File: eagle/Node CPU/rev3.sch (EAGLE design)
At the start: 44 parts, among them IC1 MEGA8-AI

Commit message: updated to revision 3 of the board
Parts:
- removed PC0, PD0: (no value), pinhead:PINHD-1X1
- removed PWR: (no value), SparkFun-Passives:JUMPER-2PTH
- removed X1: (no value), con-wago-500:W237-102
- added C5: 22pF, resistor:C-EUC0603
- added GND_1, PC8, PD8: (no value), pinhead:PINHD-1X1
- added JP1: (no value), SparkFun-Connectors:M023.5MM
- added VCC_1: VCC, pinhead:PINHD-1X1
- C1: value 0.1uF -> 22pF
- C2: value 22pF -> 0.1uF
- IC1: value MEGA8-AI -> MEGA88
- MCP1: value (none) -> MCP2515
- MCP2: value MCP2551DIL8 -> MCP2551
- renumbered MCP2551 to MCP2
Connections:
- removed net N$36: MCP2G$1.CANL, X1-2.KL
- new net N$38: MCP1D.SO, MISO.1, R3.2
- new net N$39: IC1.PB5(SCK), ISP.4, R2.1
- net GND: now also C3.2, C5.1, GND_1.1; no longer C3.1, PWR.2
- net N$1: now also C1.1, IC1.AREF; no longer IC1.PB5(SCK), MCP1D.SCK, R2.1, SCK.1
- net N$10: now also JP1.1, MCP2G$1.CANL; no longer C3.2, IC1.PB6(XTAL1/TOSC1), XTAL.2
- net N$15: now also MCP1D.SCK, R2.2, SCK.1; no longer ISP.2, R4.2
- net N$16: now also JP1.2, MCP2G$1.CANH; no longer ISP.3, R3.2
- net N$17: now also IC1.PB3(MOSI/OC2), ISP.2, R4.1; no longer ISP.4, R2.2
- net N$2: now also ISP.3; no longer MCP1D.SO, MISO.1
- net N$20: now also PC2.1; no longer PC0.1
- net N$22: now also PC5.1; no longer PC2.1
- net N$23: now also PC6.1; no longer PC3.1
- net N$24: now also PC7.1; no longer PC4.1
- net N$25: now also PC8.1; no longer PC5.1
- net N$26: now also PC4.1; no longer PC6.1
- net N$27: now also PC3.1; no longer PC7.1
- net N$28: now also PD4.1; no longer PD0.1
- net N$29: now also PD5.1; no longer PD1.1
- net N$3: now also R4.2; no longer IC1.PB3(MOSI/OC2), R4.1
- net N$30: now also PD6.1; no longer PD2.1
- net N$31: now also PD7.1; no longer PD3.1
- net N$32: now also PD8.1; no longer PD4.1
- net N$33: now also PD3.1; no longer PD5.1
- net N$34: now also PD2.1; no longer PD6.1
- net N$35: now also PD1.1; no longer PD7.1
- net N$37: now also C4.2, IC1.PB6(XTAL1/TOSC1), XTAL.1; no longer MCP2G$1.CANH, X1-1.KL
- net N$9: now also C5.2, XTAL.2; no longer C4.2, XTAL.1
- net VCC: now also C3.1, VCC_1.1; no longer C1.1, PWR.1
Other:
- moved on the sheet: C1, C2, C3, C4, ISP, MISO, MOSI, PC2, PC3, PC4, PC5, PC6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

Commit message: update rev3 schematic
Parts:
- XTAL: device special:XTAL/S -> crystal:CRYSTALHC49S
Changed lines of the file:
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@@
 <attribute name="OC_NEWARK" value="unknown"/>
 </part>
-<part name="XTAL" library="special" deviceset="XTAL/S" device="" value="8MHz">
+<part name="XTAL" library="crystal" deviceset="CRYSTAL" device="HC49S" value="8MHz">
 <attribute name="MF" value=""/>
 <attribute name="MPN" value=""/>
@@
 <wire x1="58.42" y1="45.72" x2="58.42" y2="48.26" width="0.1524" layer="91"/>
 <pinref part="XTAL" gate="G$1" pin="2"/>
-<wire x1="58.42" y1="45.72" x2="50.8" y2="45.72" width="0.1524" layer="91"/>
+<wire x1="58.42" y1="45.72" x2="50.8" y2="48.26" width="0.1524" layer="91"/>
 <pinref part="C5" gate="G$1" pin="2"/>
-<wire x1="50.8" y1="45.72" x2="43.18" y2="45.72" width="0.1524" layer="91"/>
-<junction x="50.8" y="45.72"/>
+<wire x1="50.8" y1="48.26" x2="43.18" y2="45.72" width="0.1524" layer="91"/>
+<junction x="50.8" y="48.26"/>
 </segment>
 </net>
@@
 <pinref part="C4" gate="G$1" pin="2"/>
 <pinref part="XTAL" gate="G$1" pin="1"/>
-<wire x1="43.18" y1="55.88" x2="50.8" y2="55.88" width="0.1524" layer="91"/>
+<wire x1="43.18" y1="55.88" x2="50.8" y2="53.34" width="0.1524" layer="91"/>
 <pinref part="IC1" gate="G$1" pin="PB6(XTAL1/TOSC1)"/>
 <wire x1="58.42" y1="53.34" x2="58.42" y2="55.88" width="0.1524" layer="91"/>
-<wire x1="50.8" y1="55.88" x2="58.42" y2="55.88" width="0.1524" layer="91"/>
-<junction x="50.8" y="55.88"/>
-</segment>
-</net>
+<wire x1="50.8" y1="53.34" x2="58.42" y2="55.88" width="0.1524" layer="91"/>
+<junction x="50.8" y="53.34"/>
+</segment>
+</net>

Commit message: update rev3 board schematic
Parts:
- removed PC6, PC7, PC8, PD8: (no value), pinhead:PINHD-1X1
- added ADC6, ADC7, PC0, PD0: (no value), pinhead:PINHD-1X1
- added C6, C7: 0.1uF, resistor:C-EUC0603
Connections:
- net GND: now also C6.2, C7.2, MCP1P.GND, MCP2G$2.GND
- net N$20: now also PC0.1; no longer PC2.1
- net N$22: now also PC2.1; no longer PC5.1
- net N$23: now also PC3.1; no longer PC6.1
- net N$24: now also PC4.1; no longer PC7.1
- net N$25: now also PC5.1; no longer PC8.1
- net N$26: now also ADC6.1; no longer PC4.1
- net N$27: now also ADC7.1; no longer PC3.1
- net N$28: now also PD0.1; no longer PD4.1
- net N$29: now also PD1.1; no longer PD5.1
- net N$30: now also PD2.1; no longer PD6.1
- net N$31: now also PD3.1; no longer PD7.1
- net N$32: now also PD4.1; no longer PD8.1
- net N$33: now also PD5.1; no longer PD3.1
- net N$34: now also PD6.1; no longer PD2.1
- net N$35: now also PD7.1; no longer PD1.1
- net VCC: now also C6.1, C7.1, MCP1P.VCC, MCP2G$2.VCC
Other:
- moved on the sheet: C4, C5, PC2, PC3, PC4, PC5, PD1, PD2, PD3, PD4, PD5, PD6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

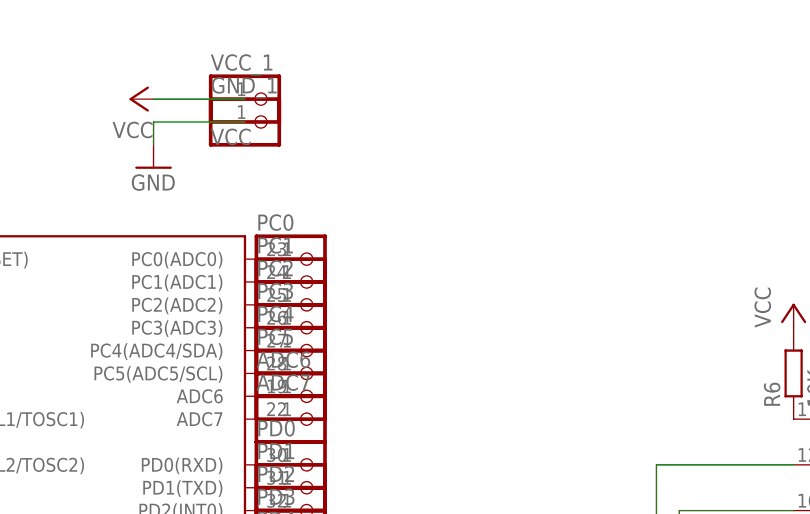
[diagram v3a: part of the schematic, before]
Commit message: add power LED to node cpu board
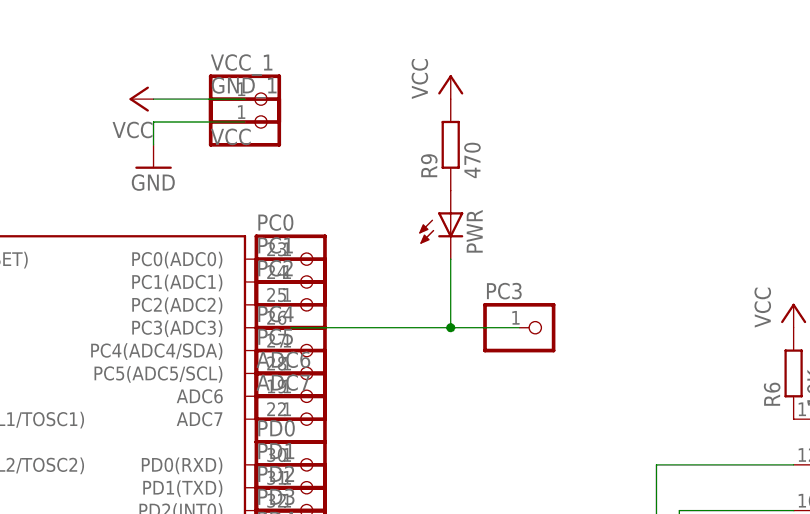
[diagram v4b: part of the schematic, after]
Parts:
- added PWR: (no value), led:LEDCHIP-LED0603
- added R9: 470, resistor:R-EU_R0603
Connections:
- removed net N$23: IC1.PC3(ADC3), PC3.1
- new net N$36: PWR.A, R9.1
- new net N$40: IC1.PC3(ADC3), PC3.1, PWR.C
- net VCC: now also R9.2
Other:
- moved on the sheet: PC3
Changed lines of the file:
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@@
 <attribute name="OC_NEWARK" value="unknown"/>
 </part>
+<part name="PWR" library="led" deviceset="LED" device="CHIP-LED0603"/>
+<part name="R9" library="resistor" deviceset="R-EU_" device="R0603" value="470">
+<attribute name="MF" value=""/>
+<attribute name="MPN" value=""/>
+<attribute name="OC_NEWARK" value="unknown"/>
+</part>
+<part name="P+11" library="supply1" deviceset="VCC" device=""/>
 </parts>
 <sheets>
@@
 <instance part="PC1" gate="G$1" x="109.22" y="68.58"/>
 <instance part="PC2" gate="G$1" x="109.22" y="66.04"/>
-<instance part="PC3" gate="G$1" x="109.22" y="63.5"/>
+<instance part="PC3" gate="G$1" x="134.62" y="63.5"/>
 <instance part="PC4" gate="G$1" x="109.22" y="60.96"/>
 <instance part="PC5" gate="G$1" x="109.22" y="58.42"/>
@@
 <attribute name="MPN" x="170.18" y="76.2" size="1.778" layer="96" rot="R180" display="off"/>
 </instance>
+<instance part="PWR" gate="G$1" x="124.46" y="76.2"/>
+<instance part="R9" gate="G$1" x="124.46" y="83.82" rot="R90">
+<attribute name="OC_NEWARK" x="124.46" y="83.82" size="1.778" layer="96" display="off"/>
+<attribute name="MF" x="124.46" y="83.82" size="1.778" layer="96" display="off"/>
+<attribute name="MPN" x="124.46" y="83.82" size="1.778" layer="96" display="off"/>
+</instance>
+<instance part="P+11" gate="VCC" x="124.46" y="91.44"/>
 </instances>
 <busses>
@@
 <pinref part="P+10" gate="VCC" pin="VCC"/>
 <junction x="228.6" y="73.66"/>
+</segment>
+<segment>
+<pinref part="R9" gate="G$1" pin="2"/>
+<pinref part="P+11" gate="VCC" pin="VCC"/>
 </segment>
 </net>
@@
 </segment>
 </net>
-<net name="N$23" class="0">
-<segment>
-<pinref part="IC1" gate="G$1" pin="PC3(ADC3)"/>
-<pinref part="PC3" gate="G$1" pin="1"/>
-</segment>
-</net>
 <net name="N$24" class="0">
 <segment>
@@
 </segment>
 </net>
+<net name="N$36" class="0">
+<segment>
+<pinref part="PWR" gate="G$1" pin="A"/>
+<pinref part="R9" gate="G$1" pin="1"/>
+</segment>
+</net>
+<net name="N$40" class="0">
+<segment>
+<pinref part="PWR" gate="G$1" pin="C"/>
+<wire x1="124.46" y1="71.12" x2="124.46" y2="63.5" width="0.1524" layer="91"/>
+<pinref part="IC1" gate="G$1" pin="PC3(ADC3)"/>
+<wire x1="124.46" y1="63.5" x2="106.68" y2="63.5" width="0.1524" layer="91"/>
+<pinref part="PC3" gate="G$1" pin="1"/>
+<wire x1="124.46" y1="63.5" x2="132.08" y2="63.5" width="0.1524" layer="91"/>
+<junction x="124.46" y="63.5"/>
+</segment>
+</net>

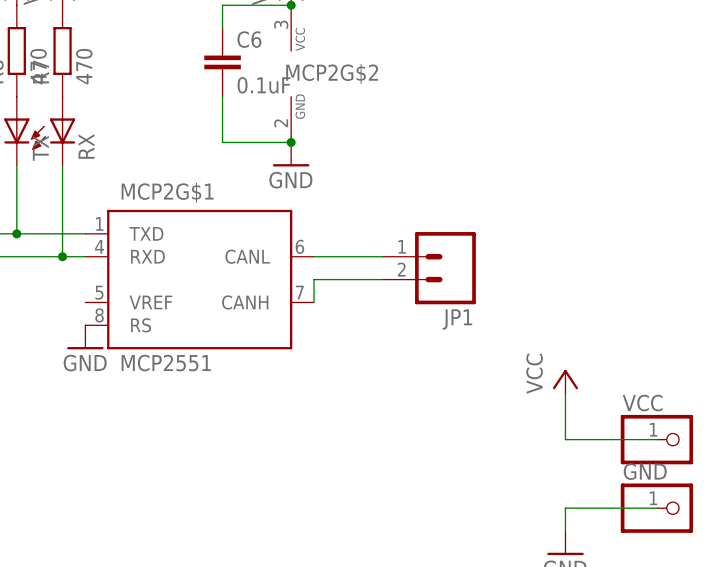
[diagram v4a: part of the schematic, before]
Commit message: nodes have custom hardware bases now
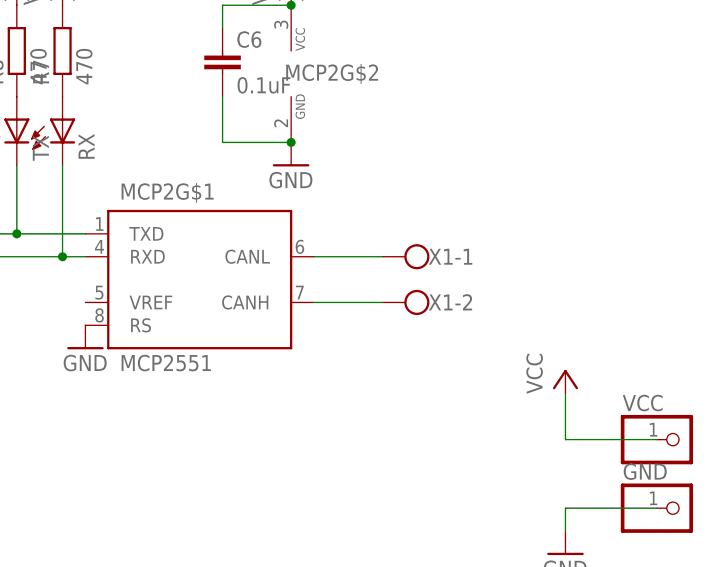
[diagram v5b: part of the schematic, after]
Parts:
- removed JP1: (no value), SparkFun-Connectors:M023.5MM
- added X1: (no value), con-wago-500:W237-102
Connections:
- net N$10: now also X1-1.KL; no longer JP1.1
- net N$16: now also X1-2.KL; no longer JP1.2
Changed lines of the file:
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@@
 </part>
 <part name="GND8" library="supply1" deviceset="GND" device=""/>
-<part name="JP1" library="SparkFun-Connectors" deviceset="M02" device="3.5MM"/>
 <part name="VCC_1" library="pinhead" deviceset="PINHD-1X1" device="" value="VCC"/>
 <part name="GND_1" library="pinhead" deviceset="PINHD-1X1" device=""/>
@@
 </part>
 <part name="P+11" library="supply1" deviceset="VCC" device=""/>
+<part name="X1" library="con-wago-500" deviceset="W237-102" device=""/>
 </parts>
 <sheets>
@@
 </instance>
 <instance part="GND8" gate="1" x="50.8" y="60.96"/>
-<instance part="JP1" gate="G$1" x="246.38" y="45.72" rot="R180"/>
 <instance part="VCC_1" gate="G$1" x="104.14" y="88.9"/>
 <instance part="GND_1" gate="G$1" x="104.14" y="86.36"/>
@@
 </instance>
 <instance part="P+11" gate="VCC" x="124.46" y="91.44"/>
+<instance part="X1" gate="-1" x="243.84" y="45.72" rot="R180"/>
+<instance part="X1" gate="-2" x="243.84" y="40.64" rot="R180"/>
 </instances>
 <busses>
@@
 <segment>
 <pinref part="MCP2" gate="G$1" pin="CANL"/>
-<pinref part="JP1" gate="G$1" pin="1"/>
 <wire x1="231.14" y1="45.72" x2="238.76" y2="45.72" width="0.1524" layer="91"/>
-</segment>
-</net>
-<net name="N$16" class="0">
-<segment>
-<pinref part="MCP2" gate="G$1" pin="CANH"/>
-<wire x1="231.14" y1="40.64" x2="231.14" y2="43.18" width="0.1524" layer="91"/>
-<pinref part="JP1" gate="G$1" pin="2"/>
-<wire x1="231.14" y1="43.18" x2="238.76" y2="43.18" width="0.1524" layer="91"/>
+<pinref part="X1" gate="-1" pin="KL"/>
 </segment>
 </net>
@@
 </segment>
 </net>
+<net name="N$16" class="0">
+<segment>
+<pinref part="MCP2" gate="G$1" pin="CANH"/>
+<pinref part="X1" gate="-2" pin="KL"/>
+<wire x1="231.14" y1="40.64" x2="238.76" y2="40.64" width="0.1524" layer="91"/>
+</segment>
+</net>
